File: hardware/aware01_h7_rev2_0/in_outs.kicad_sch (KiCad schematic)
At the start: 28 parts, among them J3 InL, J4 InR, J5 OutL, J6 OutR, U10 NE5532DRG4, U11 NE5532DRG4

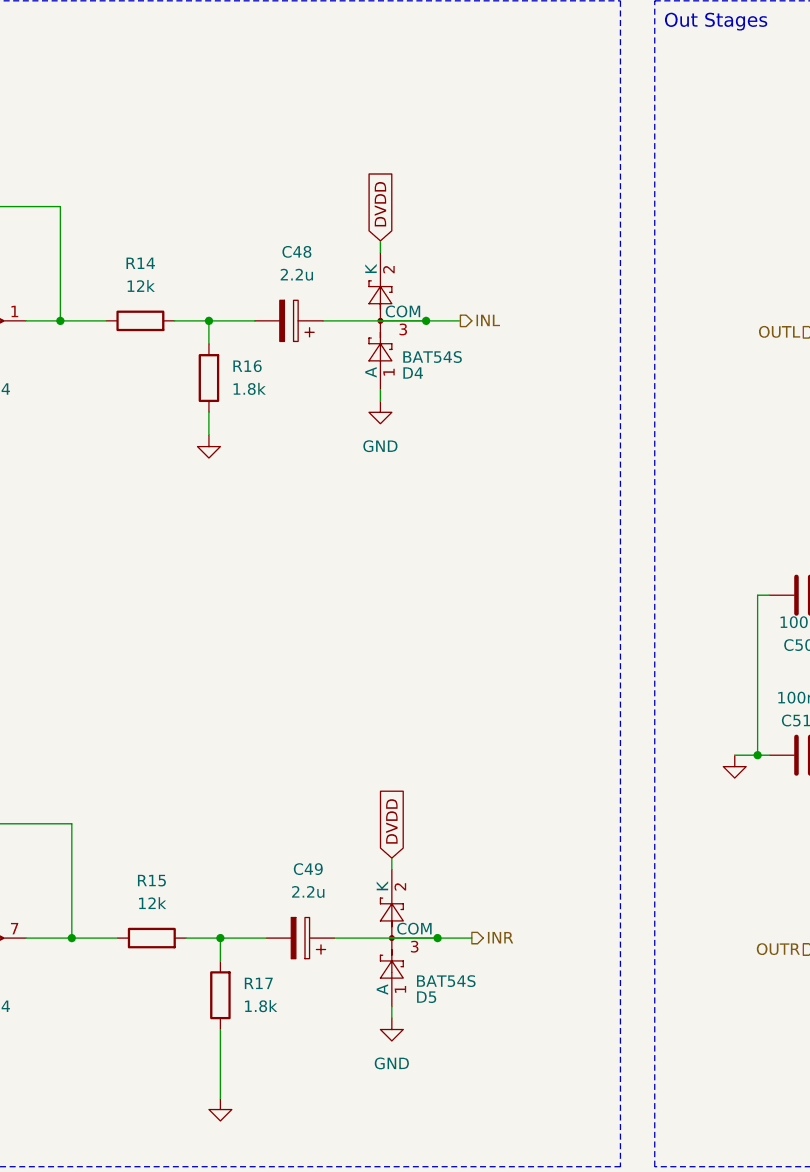
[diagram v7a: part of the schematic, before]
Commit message: hardware: change clamping reference to codec AVDD
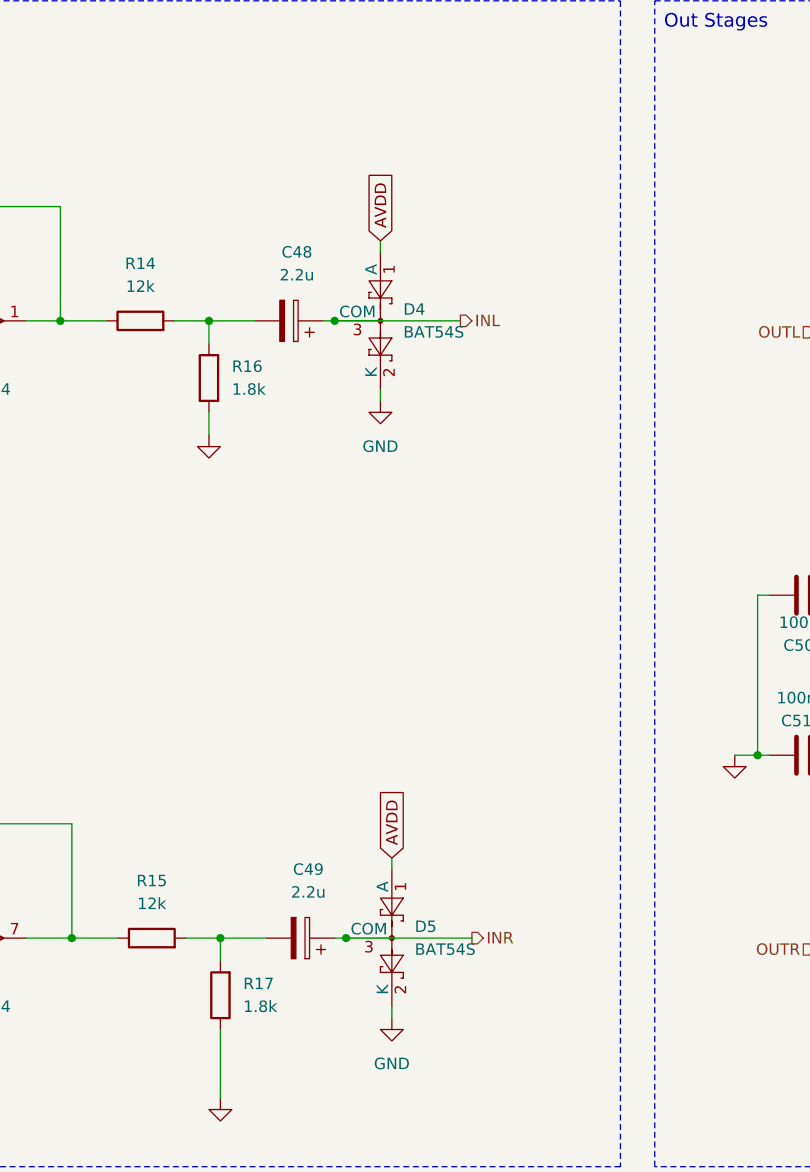
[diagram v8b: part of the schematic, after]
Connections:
- net DVDD is gone; now on net GND: D4.2 (K), D5.2 (K)
- net GND: no longer D4.1 (A), D5.1 (A)
- new net AVDD: D4.1 (A), D5.1 (A)
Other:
- moved on the sheet: D4, D5
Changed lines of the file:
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@@
 	)
 	(junction
-		(at 124.46 64.77)
-		(diameter 0)
-		(color 0 0 0 0)
-	)
-	(junction
 		(at 204.47 66.04)
 		(diameter 0)
@@
 	)
 	(junction
-		(at 34.29 110.49)
+		(at 115.57 133.35)
 		(diameter 0)
 		(color 0 0 0 0)
 	)
 	(junction
-		(at 125.73 133.35)
+		(at 34.29 110.49)
 		(diameter 0)
 		(color 0 0 0 0)
@@
 	)
 	(junction
+		(at 114.3 64.77)
+		(diameter 0)
+		(color 0 0 0 0)
+	)
+	(junction
 		(at 161.29 113.03)
 		(diameter 0)
@@
 	(wire
 		(pts
+			(xy 114.3 64.77) (xy 128.27 64.77)
+		)
+		(stroke
+			(width 0)
+			(type default)
+		)
+	)
+	(wire
+		(pts
 			(xy 31.75 110.49) (xy 34.29 110.49)
 		)
@@
 	(wire
 		(pts
+			(xy 115.57 133.35) (xy 129.54 133.35)
+		)
+		(stroke
+			(width 0)
+			(type default)
+		)
+	)
+	(wire
+		(pts
 			(xy 246.38 71.12) (xy 243.84 71.12)
 		)
@@
 	(wire
 		(pts
-			(xy 113.03 64.77) (xy 124.46 64.77)
+			(xy 113.03 64.77) (xy 114.3 64.77)
 		)
 		(stroke
@@
 	(wire
 		(pts
-			(xy 124.46 64.77) (xy 128.27 64.77)
-		)
-		(stroke
-			(width 0)
-			(type default)
-		)
-	)
-	(wire
-		(pts
 			(xy 45.72 135.89) (xy 64.77 135.89)
 		)
@@
 	(wire
 		(pts
-			(xy 114.3 133.35) (xy 125.73 133.35)
+			(xy 114.3 133.35) (xy 115.57 133.35)
 		)
 		(stroke
@@
 	(wire
 		(pts
-			(xy 125.73 133.35) (xy 129.54 133.35)
-		)
-		(stroke
-			(width 0)
-			(type default)
-		)
-	)
-	(wire
-		(pts
 			(xy 172.72 93.98) (xy 172.72 95.25)
 		)
@@
 		)
 	)
-	(global_label "DVDD"
+	(global_label "AVDD"
 		(shape input)
 		(at 119.38 55.88 90)
@@
 		)
 		(property "Intersheetrefs" "${INTERSHEET_REFS}"
-			(at 119.38 47.9962 90)
+			(at 119.38 48.1776 90)
 			(effects
 				(font
@@
 		)
 	)
-	(global_label "DVDD"
+	(global_label "AVDD"
 		(shape input)
 		(at 120.65 124.46 90)
@@
 		)
 		(property "Intersheetrefs" "${INTERSHEET_REFS}"
-			(at 120.65 116.5762 90)
+			(at 120.65 116.7576 90)
 			(effects
 				(font
@@
 	(symbol
 		(lib_id "Diode:BAT54S")
-		(at 119.38 64.77 90)
+		(at 119.38 64.77 270)
 		(unit 1)
 		(exclude_from_sim no)
@@
 		(on_board yes)
 		(dnp no)
+		(fields_autoplaced yes)
 		(property "Reference" "D4"
-			(at 124.206 70.612 90)
+			(at 121.92 63.4999 90)
 			(effects
 				(font
@@
 		)
 		(property "Value" "BAT54S"
-			(at 128.524 68.834 90)
+			(at 121.92 66.0399 90)
 			(effects
 				(font
@@
 		)
 		(property "Footprint" "Package_TO_SOT_SMD:SOT-23"
-			(at 116.205 62.865 0)
+			(at 122.555 66.675 0)
 			(effects
 				(font
@@
 		)
 		(property "Datasheet" "https://www.diodes.com/assets/Datasheets/ds11005.pdf"
-			(at 119.38 67.818 0)
+			(at 119.38 61.722 0)
 			(effects
 				(font
@@
 	(symbol
 		(lib_id "Diode:BAT54S")
-		(at 120.65 133.35 90)
+		(at 120.65 133.35 270)
 		(unit 1)
 		(exclude_from_sim no)
@@
 		(on_board yes)
 		(dnp no)
+		(fields_autoplaced yes)
 		(property "Reference" "D5"
-			(at 125.73 139.954 90)
+			(at 123.19 132.0799 90)
 			(effects
 				(font
@@
 		)
 		(property "Value" "BAT54S"
-			(at 130.048 138.176 90)
+			(at 123.19 134.6199 90)
 			(effects
 				(font
@@
 		)
 		(property "Footprint" "Package_TO_SOT_SMD:SOT-23"
-			(at 117.475 131.445 0)
+			(at 123.825 135.255 0)
 			(effects
 				(font
@@
 		)
 		(property "Datasheet" "https://www.diodes.com/assets/Datasheets/ds11005.pdf"
-			(at 120.65 136.398 0)
+			(at 120.65 130.302 0)
 			(effects
 				(font
